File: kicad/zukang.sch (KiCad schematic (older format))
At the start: 118 parts, among them J1 RX, J2 TX, Q1 BC547, Q2 BC547, Q3 BC547, SW1 SW_Push, SW2 SW_Push, U1 74HC595, U10 F5161BS, U11 TL084, U12 TL084, U13 L7805, U14 L7905, U15 LM1117-3.3, U16 STM32F030F4P6, U17 STM32F030F4P6, U18 ne602, U2 74HC595, U3 ne602, U4 F5161BS, U5 ne602, U6 CD4052B, U7 F5161BS, U8 F5161BS, U9 F5161BS, Y1 8M, Y2 8M

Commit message: 改电阻
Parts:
- removed R16, R21: 100, symbol Device:R
- removed R20: 1K, symbol Device:R
- R17: value 100 -> 66.5
- R18: value 170 -> 6.65K
- R19: value 50 -> 100
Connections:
- net GND: no longer R17.2
- net at R18.2, R19.1: now also C5.2
- net at C1.2, R14.1: now also R17.1
- net at C2.2, R15.1: now also R17.2; no longer R17.1
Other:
- moved on the sheet: R17, R19
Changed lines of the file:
@@
 P 3700 5600
 F 0 "R18" H 3770 5646 50  0000 L CNN
-F 1 "170" H 3770 5555 50  0000 L CNN
+F 1 "6.65K" H 3770 5555 50  0000 L CNN
 F 2 "" V 3630 5600 50  0001 C CNN
 F 3 "~" H 3700 5600 50  0001 C CNN
@@
 L Device:R R19
 U 1 1 5F1F005E
-P 3700 6100
-F 0 "R19" H 3770 6146 50  0000 L CNN
-F 1 "50" H 3770 6055 50  0000 L CNN
-F 2 "" V 3630 6100 50  0001 C CNN
-F 3 "~" H 3700 6100 50  0001 C CNN
-	1    3700 6100
+P 3700 6050
+F 0 "R19" H 3770 6096 50  0000 L CNN
+F 1 "100" H 3770 6005 50  0000 L CNN
+F 2 "" V 3630 6050 50  0001 C CNN
+F 3 "~" H 3700 6050 50  0001 C CNN
+	1    3700 6050
 	1    0    0    -1
 $EndComp
@@
 	5150 6250 5300 6250
 $Comp
-L Device:R R21
-U 1 1 5F2BA0DD
-P 4450 6000
-F 0 "R21" H 4520 6046 50  0000 L CNN
-F 1 "100" H 4520 5955 50  0000 L CNN
-F 2 "" V 4380 6000 50  0001 C CNN
-F 3 "~" H 4450 6000 50  0001 C CNN
-	1    4450 6000
-	1    0    0    -1
-$EndComp
-$Comp
-L Device:R R20
-U 1 1 5F2BC1B9
-P 4150 5850
-F 0 "R20" V 3943 5850 50  0000 C CNN
-F 1 "1K" V 4034 5850 50  0000 C CNN
-F 2 "" V 4080 5850 50  0001 C CNN
-F 3 "~" H 4150 5850 50  0001 C CNN
-	1    4150 5850
-	0    1    1    0
-$EndComp
-Wire Wire Line
-	4300 5850 4450 5850
-Wire Wire Line
-	4000 5850 3700 5850
-Wire Wire Line
-	3700 5850 3700 5950
-Wire Wire Line
-	3700 5750 3700 5850
-Connection ~ 3700 5850
-$Comp
 L power:GND #PWR0124
 U 1 1 5F3ADD0B
-P 3700 6250
-F 0 "#PWR0124" H 3700 6000 50  0001 C CNN
-F 1 "GND" H 3705 6077 50  0000 C CNN
-F 2 "" H 3700 6250 50  0001 C CNN
-F 3 "" H 3700 6250 50  0001 C CNN
-	1    3700 6250
-	1    0    0    -1
-$EndComp
-$Comp
-L power:GND #PWR0125
-U 1 1 5F3AF2F7
-P 4450 6400
-F 0 "#PWR0125" H 4450 6150 50  0001 C CNN
-F 1 "GND" H 4455 6227 50  0000 C CNN
-F 2 "" H 4450 6400 50  0001 C CNN
-F 3 "" H 4450 6400 50  0001 C CNN
-	1    4450 6400
+P 3700 6400
+F 0 "#PWR0124" H 3700 6150 50  0001 C CNN
+F 1 "GND" H 3705 6227 50  0000 C CNN
+F 2 "" H 3700 6400 50  0001 C CNN
+F 3 "" H 3700 6400 50  0001 C CNN
+	1    3700 6400
 	1    0    0    -1
 $EndComp
@@
 Wire Wire Line
 	4450 5750 4450 5850
-Connection ~ 4450 5850
-Wire Wire Line
-	4750 6200 4450 6200
-Wire Wire Line
-	4450 6200 4450 6150
-Wire Wire Line
-	4450 6400 4450 6200
-Connection ~ 4450 6200
 Wire Wire Line
 	2450 5500 2450 5450
@@
 L Device:R R17
 U 1 1 5FD314D2
-P 3100 8900
-F 0 "R17" H 3170 8946 50  0000 L CNN
-F 1 "100" H 3170 8855 50  0000 L CNN
-F 2 "" V 3030 8900 50  0001 C CNN
-F 3 "~" H 3100 8900 50  0001 C CNN
-	1    3100 8900
-	1    0    0    -1
-$EndComp
-$Comp
-L Device:R R16
-U 1 1 5FD32E29
-P 3000 7700
-F 0 "R16" H 3070 7746 50  0000 L CNN
-F 1 "100" H 3070 7655 50  0000 L CNN
-F 2 "" V 2930 7700 50  0001 C CNN
-F 3 "~" H 3000 7700 50  0001 C CNN
-	1    3000 7700
+P 3050 8200
+F 0 "R17" H 3120 8246 50  0000 L CNN
+F 1 "66.5" H 3120 8155 50  0000 L CNN
+F 2 "" V 2980 8200 50  0001 C CNN
+F 3 "~" H 3050 8200 50  0001 C CNN
+	1    3050 8200
 	1    0    0    -1
 $EndComp
@@
 $EndComp
 $Comp
-L power:GND #PWR0131
-U 1 1 5FD3726E
-P 3000 7500
-F 0 "#PWR0131" H 3000 7250 50  0001 C CNN
-F 1 "GND" H 3005 7327 50  0000 C CNN
-F 2 "" H 3000 7500 50  0001 C CNN
-F 3 "" H 3000 7500 50  0001 C CNN
-	1    3000 7500
-	-1   0    0    1
-$EndComp
-$Comp
 L power:GND #PWR0132
 U 1 1 5FD38994
@@
 	1    0    0    -1
 $EndComp
-Wire Wire Line
-	3000 7550 3000 7500
-Wire Wire Line
-	3000 7850 3000 7900
-Wire Wire Line
-	2800 7900 3000 7900
-Connection ~ 3000 7900
-Wire Wire Line
-	3000 7900 3350 7900
-Wire Wire Line
-	2850 8550 3100 8550
-Wire Wire Line
-	3100 8750 3100 8550
-Connection ~ 3100 8550
-Wire Wire Line
-	3100 8550 3350 8550
 Wire Wire Line
 	3650 7900 4200 7900
@@
 Wire Wire Line
 	2650 6200 2650 6350
+Wire Wire Line
+	4750 6200 4750 6400
+Wire Wire Line
+	4750 6400 3700 6400
+Wire Wire Line
+	3700 6200 3700 6400
+Connection ~ 3700 6400
+Wire Wire Line
+	3700 5750 3700 5850
+Wire Wire Line
+	3700 5850 4450 5850
+Connection ~ 3700 5850
+Wire Wire Line
+	3700 5850 3700 5900
+Wire Wire Line
+	3350 7900 3050 7900
+Wire Wire Line
+	3350 8550 3050 8550
+Wire Wire Line
+	3050 8050 3050 7900
+Connection ~ 3050 7900
+Wire Wire Line
+	3050 7900 2800 7900
+Wire Wire Line
+	3050 8350 3050 8550
+Connection ~ 3050 8550
+Wire Wire Line
+	3050 8550 2850 8550
 $EndSCHEMATC

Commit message: 改电路
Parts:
- removed C30: 104, symbol Device:C
- added Q4: BC547, Package_TO_SOT_THT:TO-92_Inline, symbol Transistor_BJT:BC547
- added Q5: BC557, Package_TO_SOT_THT:TO-92_Inline, symbol Transistor_BJT:BC557
- added R16: R, symbol Device:R
- R14, R15: value 1K -> 500
- R17: value 66.5 -> 100
- R18: value 6.65K -> 500
- R19: value 100 -> 20
- R5: value 100 -> 1K
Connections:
- net +5V: now also Q4.1 (C)
- net PWM1: now also R3.1, R6.1, Q4.3 (E), Q5.3 (E); no longer R5.1
- net at U17.18 (PA10): now also R16.2
- net at C1.2, R14.1, R17.1: now also R5.1
- net at C2.2, R15.1, R17.2: now also R5.2
- new net: Q4.2 (B), Q5.2 (B), R16.1
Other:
- moved on the sheet: C21, C25, C26, R14, R15, R47, U17, Y2

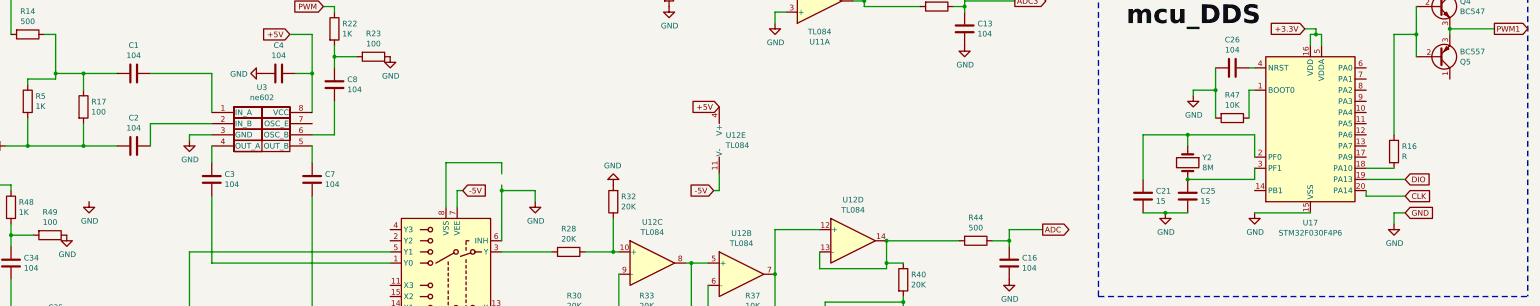
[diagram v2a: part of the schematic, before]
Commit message: 电路改错
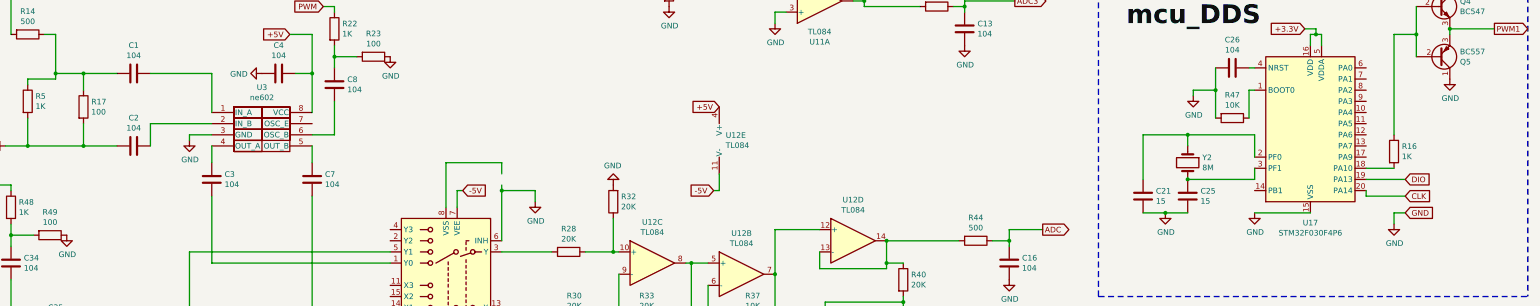
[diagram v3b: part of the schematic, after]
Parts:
- R16: value R -> 1K
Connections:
- net GND: now also Q5.1 (C)
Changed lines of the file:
@@
 	0    1    1    0
-$EndComp
-$Comp
-L power:GND #PWR0132
-U 1 1 5FD38994
-P 3100 9050
-F 0 "#PWR0132" H 3100 8800 50  0001 C CNN
-F 1 "GND" H 3105 8877 50  0000 C CNN
-F 2 "" H 3100 9050 50  0001 C CNN
-F 3 "" H 3100 9050 50  0001 C CNN
-	1    3100 9050
-	1    0    0    -1
 $EndComp
 Wire Wire Line
@@
 P 14800 8600
 F 0 "R16" H 14870 8646 50  0000 L CNN
-F 1 "R" H 14870 8555 50  0000 L CNN
+F 1 "1K" H 14870 8555 50  0000 L CNN
 F 2 "" V 14730 8600 50  0001 C CNN
 F 3 "~" H 14800 8600 50  0001 C CNN
@@
 Wire Wire Line
 	2450 5800 2650 5800
+$Comp
+L power:GND #PWR?
+U 1 1 5E722693
+P 15300 7950
+F 0 "#PWR?" H 15300 7700 50  0001 C CNN
+F 1 "GND" H 15305 7777 50  0000 C CNN
+F 2 "" H 15300 7950 50  0001 C CNN
+F 3 "" H 15300 7950 50  0001 C CNN
+	1    15300 7950
+	1    0    0    -1
+$EndComp
 $EndSCHEMATC
